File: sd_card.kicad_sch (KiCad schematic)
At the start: 19 parts, among them J5 Screw_Terminal_01x03, J702 DM3AT-SF-PEJM5_40_, U11 EMIF06-MSD02N16, U701 ADM2565EBRNZ

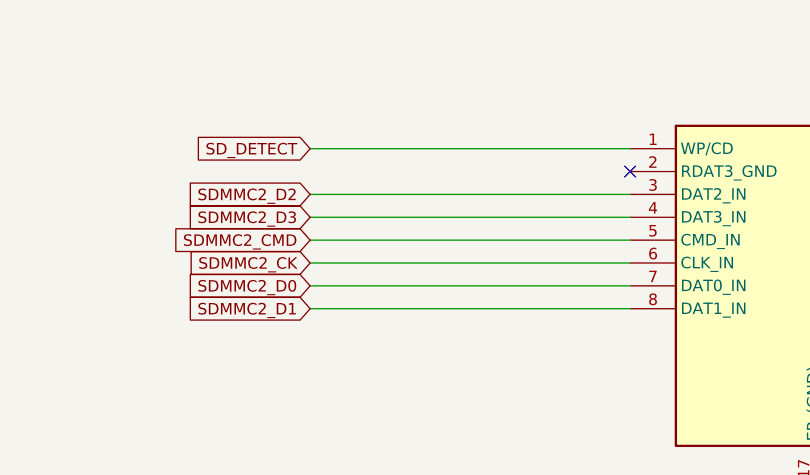
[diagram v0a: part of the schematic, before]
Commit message: fine tune high speed traces
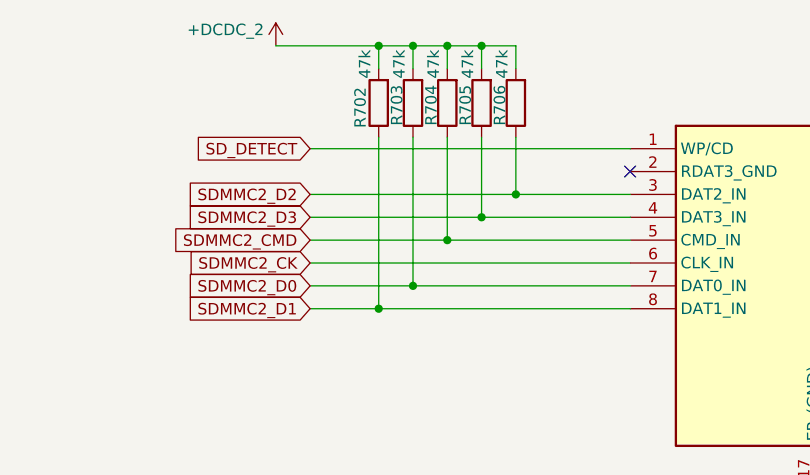
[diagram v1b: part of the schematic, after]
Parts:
- added R702, R703, R704, R705, R706: 47k, Resistor_SMD:R_0402_1005Metric, symbol Device:R
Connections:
- net +DCDC_2: now also R702.2, R703.2, R704.2, R705.2, R706.2
- net SDMMC2_CMD: now also R704.1
- net SDMMC2_D0: now also R703.1
- net SDMMC2_D1: now also R702.1
- net SDMMC2_D2: now also R706.1
- net SDMMC2_D3: now also R705.1

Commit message: minor design improvements
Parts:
- removed R702, R703, R704, R705, R706: 47k, Resistor_SMD:R_0402_1005Metric, symbol Device:R
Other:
- note added: "Provides internal 90K Ohm pull-up"
